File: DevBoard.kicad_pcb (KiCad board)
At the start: 4 copper layers, 100 x 83.4 mm, 130 parts, among them J1 MCUToAudio1, J10 Jumper, J11 RJ45, J12 Jumper, J13 Jumper, J14 Jumper, J15 Jumper, J16 Jumper, J17 Jumper, J18 DAC_I2S, J19 DAC_OUT, J2 MCUToAudio1, J20 DAC_Amplified, J21 DAC_Amplified, J22 Voltmeter, J23 Ground, J25 Interconnects, J26 DAC_I2S, J3 MCUToAudio2, J30 CV_Scaled_Out1, J31 AudioToMCU1, J32 AudioToMCU2, J33 CV_In2, J35 Power, J39 Ground, J4 MCUToAudio2, J40 Ground, J41 Ground, J44 Pot1, J45 Pot2, J46 Pot3, J47 Pot4, J48 CV_In1, J49 CV_Scaled_Out2, J5 MCUToCV1, J50 AudioToMCU1, J51 AudioToMCU2, J52 Pot_Out, J6 MCUToCV1, J7 MCUToCV2, J8 MCUToCV2, J9 Jumper, SW2 SW_DPDT_x2, U1 MCP6004, U2 TL074, U3 LM1117-3.3, U4 LM1117-5.0, U5 LM4040DBZ-5, U6 PCM5100APW, U8 TL072

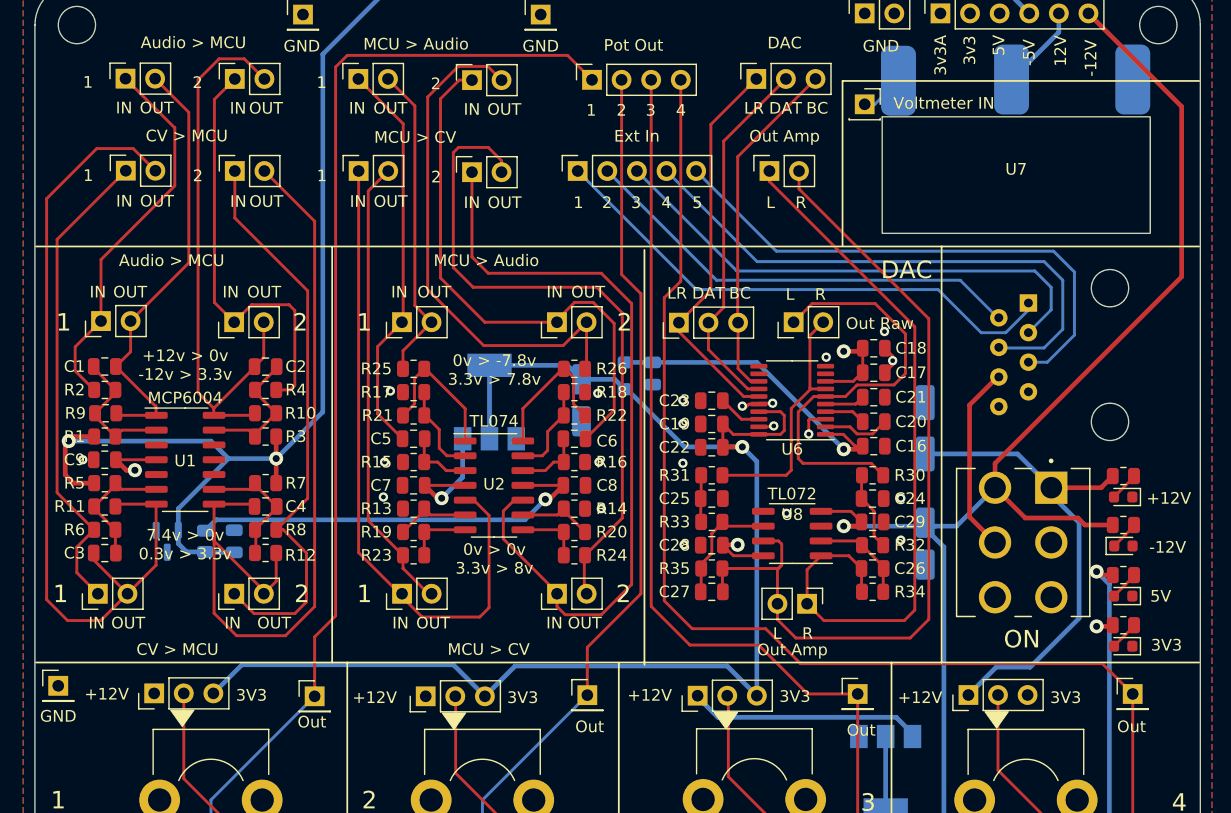
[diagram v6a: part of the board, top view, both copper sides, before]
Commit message: Layout tweaks
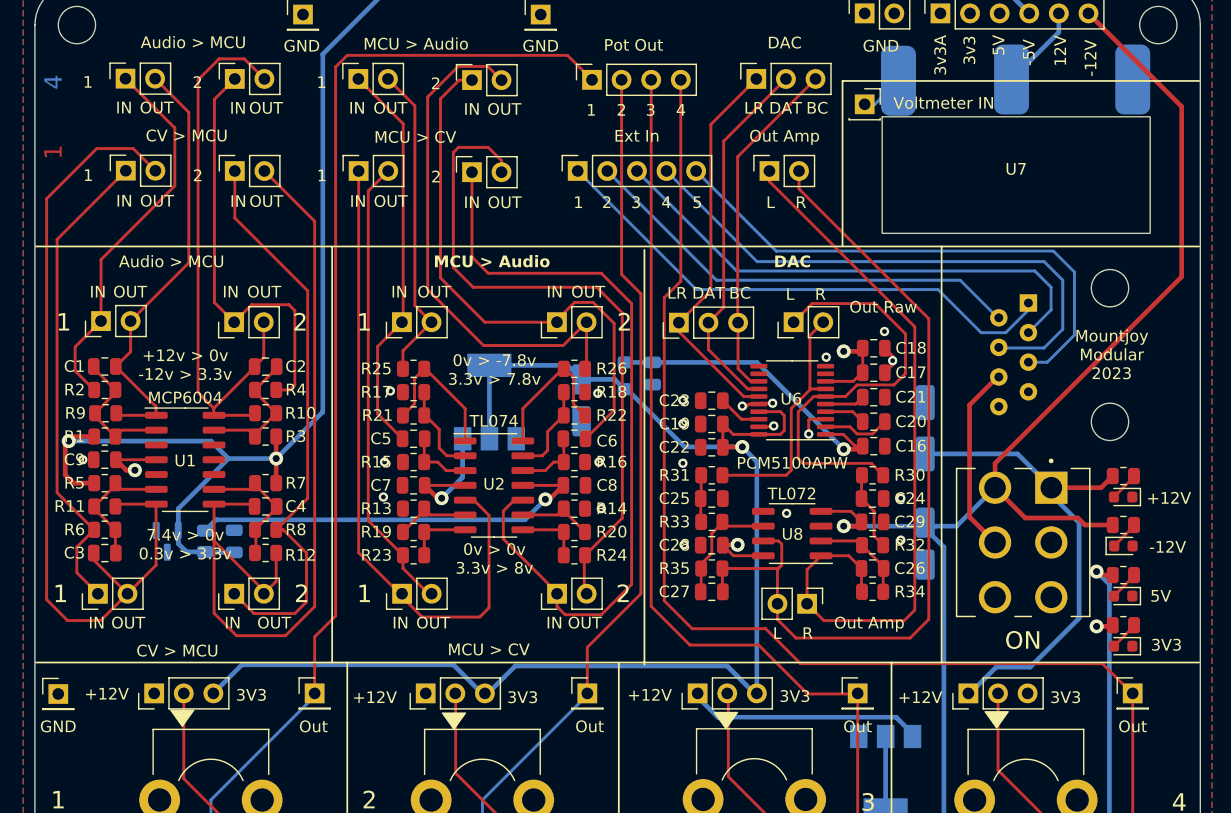
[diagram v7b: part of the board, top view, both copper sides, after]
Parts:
- added FID1: Fiducial, Custom_Footprints:4_Layer_Markers, F.Cu at (51.6, 78.1)
- moved J41 0.70 mm to (52.0, 127.6)
- moved J12 0.25 mm to (83.5, 127.5)
- moved J44 0.25 mm to (74.0, 127.5)
- moved J14 0.20 mm to (106.9, 127.5)
- moved J45 0.15 mm to (97.4, 127.5)
- moved J16 0.14 mm to (130.1, 127.5)
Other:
- board text added: "Mountjoy Modular 2023"
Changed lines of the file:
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@@
   )
   (footprint "Connector_PinHeader_2.54mm:PinHeader_1x01_P2.54mm_Vertical" (layer "F.Cu")
-    (at 52 126.9)
+    (at 52 127.6)
     (descr "Through hole straight pin header, 1x01, 2.54mm pitch, single row")
     (tags "Through hole pin header THT 1x01 2.54mm single row")
@@
   )
   (footprint "Connector_PinHeader_2.54mm:PinHeader_1x01_P2.54mm_Vertical" (layer "F.Cu")
-    (at 144.2 127.6)
+    (at 144.2 127.55)
     (descr "Through hole straight pin header, 1x01, 2.54mm pitch, single row")
     (tags "Through hole pin header THT 1x01 2.54mm single row")
@@
     (property "ki_keywords" "audio dac 2ch 32bit 384kHz")
     (attr smd)
-    (fp_text reference "U6" (at 0 -4.2 180) (layer "F.SilkS")
+    (fp_text reference "U6" (at 0.08 0.1 180) (layer "F.SilkS")
         (effects (font (size 1 1) (thickness 0.15)))
     )
-    (fp_text value "PCM5100APW" (at 0 4.2 180) (layer "F.Fab")
+    (fp_text value "PCM5100APW" (at 0 -5.4 180) (layer "F.SilkS")
         (effects (font (size 1 1) (thickness 0.15)))
     )
@@
   )
   (footprint "Connector_PinHeader_2.54mm:PinHeader_1x03_P2.54mm_Vertical" (layer "F.Cu")
-    (at 83.53 127.8 90)
+    (at 83.53 127.55 90)
     (descr "Through hole straight pin header, 1x03, 2.54mm pitch, single row")
     (tags "Through hole pin header THT 1x03 2.54mm single row")
@@
   )
   (footprint "Connector_PinHeader_2.54mm:PinHeader_1x03_P2.54mm_Vertical" (layer "F.Cu")
-    (at 106.865 127.749665 90)
+    (at 106.865 127.55 90)
     (descr "Through hole straight pin header, 1x03, 2.54mm pitch, single row")
     (tags "Through hole pin header THT 1x03 2.54mm single row")
@@
     (property "ki_keywords" "dual opamp")
     (attr smd)
-    (fp_text reference "U8" (at 0 1.635) (layer "F.SilkS")
+    (fp_text reference "U8" (at -0.02 -0.065) (layer "F.SilkS")
         (effects (font (size 1 1) (thickness 0.15)))
     )
@@
   )
   (footprint "Connector_PinHeader_2.54mm:PinHeader_1x01_P2.54mm_Vertical" (layer "F.Cu")
-    (at 97.4 127.7)
+    (at 97.4 127.55)
     (descr "Through hole straight pin header, 1x01, 2.54mm pitch, single row")
     (tags "Through hole pin header THT 1x01 2.54mm single row")
@@
   )
   (footprint "Connector_PinHeader_2.54mm:PinHeader_1x01_P2.54mm_Vertical" (layer "F.Cu")
-    (at 120.6 127.6)
+    (at 120.6 127.55)
     (descr "Through hole straight pin header, 1x01, 2.54mm pitch, single row")
     (tags "Through hole pin header THT 1x01 2.54mm single row")
@@
   )
   (footprint "Connector_PinHeader_2.54mm:PinHeader_1x01_P2.54mm_Vertical" (layer "F.Cu")
-    (at 74 127.8)
+    (at 74 127.55)
     (descr "Through hole straight pin header, 1x01, 2.54mm pitch, single row")
     (tags "Through hole pin header THT 1x01 2.54mm single row")
@@
   )
   (footprint "Connector_PinHeader_2.54mm:PinHeader_1x03_P2.54mm_Vertical" (layer "F.Cu")
-    (at 130.1 127.688915 90)
+    (at 130.1 127.55 90)
     (descr "Through hole straight pin header, 1x03, 2.54mm pitch, single row")
     (tags "Through hole pin header THT 1x03 2.54mm single row")
@@
     )
   )
+  (footprint "Custom_Footprints:4_Layer_Markers" (layer "F.Cu")
+    (at 51.6 78.1 90)
+    (property "Sheetfile" "DevBoard.kicad_sch")
+    (property "Sheetname" "")
+    (property "ki_description" "Fiducial Marker")
+    (property "ki_keywords" "fiducial marker")
+    (attr through_hole)
+    (fp_text reference "FID1" (at 0 4 90) (layer "F.SilkS") hide
+        (effects (font (size 1 1) (thickness 0.15)))
+    )
+    (fp_text value "Fiducial" (at 0 -4 90) (layer "F.Fab")
+        (effects (font (size 1 1) (thickness 0.15)))
+    )
+    (fp_text user "1" (at -3 0 90) (layer "F.Cu")
+        (effects (font (size 1.5 1.5) (thickness 0.3)))
+    )
+    (fp_text user "2" (at -1 0 90) (layer "In1.Cu")
+        (effects (font (size 1.5 1.5) (thickness 0.3)))
+    )
+    (fp_text user "3" (at 1 0 90) (layer "In2.Cu")
+        (effects (font (size 1.5 1.5) (thickness 0.3)))
+    )
+    (fp_text user "4" (at 3 0 90) (layer "B.Cu")
+        (effects (font (size 1.5 1.5) (thickness 0.3)))
+    )
+    (fp_poly
+      (pts
+        (xy 4 1)
+        (xy -4 1)
+        (xy -4 -1)
+        (xy 4 -1)
+      )
+      (stroke (width 0.1) (type solid)) (fill solid) (layer "B.Mask"))
+    (fp_poly
+      (pts
+        (xy 4 1)
+        (xy -4 1)
+        (xy -4 -1)
+        (xy 4 -1)
+      )
+      (stroke (width 0.1) (type solid)) (fill solid) (layer "F.Mask"))
+    (zone (net 0) (net_name "") (layers "*.Cu") (hatch edge 0.508)
+      (connect_pads (clearance 0))
+      (min_thickness 0.254) (filled_areas_thickness no)
+      (keepout (tracks not_allowed) (vias not_allowed) (pads allowed) (copperpour not_allowed) (footprints allowed))
+      (fill (thermal_gap 0.508) (thermal_bridge_width 0.508))
+      (polygon
+        (pts
+          (xy 52.7 74)
+          (xy 52.7 82.2)
+          (xy 50.5 82.2)
+          (xy 50.5 74)
+        )
+      )
+    )
+  )
   (footprint "Capacitor_SMD:CP_Elec_5x5.4" (layer "B.Cu")
     (at 126.4 104.8 90)
@@
     (effects (font (size 1 1) (thickness 0.15)) (justify bottom))
   )
-  (gr_text "Out" (at 144.1 131) (layer "F.SilkS")
+  (gr_text "Out" (at 144.2 131) (layer "F.SilkS")
     (effects (font (size 1 1) (thickness 0.15)) (justify bottom))
   )
@@
     (effects (font (size 1 1) (thickness 0.15)) (justify bottom))
   )
-  (gr_text "Out Amp" (at 115 124.4) (layer "F.SilkS")
+  (gr_text "Out Amp" (at 121.6 122.1) (layer "F.SilkS")
     (effects (font (size 1 1) (thickness 0.15)) (justify bottom))
   )
@@
     (effects (font (size 1 1) (thickness 0.15)) (justify bottom))
   )
-  (gr_text "ON" (at 134.7 123.7875) (layer "F.SilkS" knockout)
+  (gr_text "ON" (at 134.8 123.9) (layer "F.SilkS" knockout)
     (effects (font (size 1.5 1.5) (thickness 0.2)) (justify bottom))
   )
@@
     (effects (font (size 1 1) (thickness 0.15)) (justify bottom))
   )
-  (gr_text "Out" (at 73.765 130.600335) (layer "F.SilkS")
+  (gr_text "Out" (at 73.9 131) (layer "F.SilkS")
     (effects (font (size 1 1) (thickness 0.15)) (justify bottom))
   )
@@
     (effects (font (size 1 1) (thickness 0.15)) (justify bottom))
   )
-  (gr_text "MCU > CV" (at 85.4 124.3675) (layer "F.SilkS" knockout)
-    (effects (font (size 1 1) (thickness 0.15)) (justify left bottom))
+  (gr_text "MCU > CV" (at 85.4 124.4) (layer "F.SilkS" knockout)
+    (effects (font (size 1 1) (thickness 0.2)) (justify left bottom))
   )
   (gr_text "2" (at 63.975 83.725) (layer "F.SilkS" knockout)
@@
     (effects (font (size 1 1) (thickness 0.15)) (justify bottom))
   )
-  (gr_text "DAC" (at 124.8 92.1) (layer "F.SilkS" knockout)
-    (effects (font (size 1.5 1.5) (thickness 0.3)) (justify bottom))
+  (gr_text "DAC" (at 115 91.1) (layer "F.SilkS" knockout)
+    (effects (font (size 1 1) (thickness 0.2) bold) (justify bottom))
   )
   (gr_text "IN" (at 67.45 85.925) (layer "F.SilkS")
@@
     (effects (font (size 1 1) (thickness 0.15)) (justify bottom))
   )
-  (gr_text "CV > MCU" (at 58.7 124.3675) (layer "F.SilkS" knockout)
-    (effects (font (size 1 1) (thickness 0.15)) (justify left bottom))
+  (gr_text "CV > MCU" (at 58.7 124.5) (layer "F.SilkS" knockout)
+    (effects (font (size 1 1) (thickness 0.2)) (justify left bottom))
   )
   (gr_text "IN" (at 81.3675 122.1) (layer "F.SilkS")
@@
     (effects (font (size 1 1) (thickness 0.15)) (justify bottom))
   )
-  (gr_text "Out Raw" (at 122.5 96.4) (layer "F.SilkS")
+  (gr_text "Out Raw" (at 122.8 95) (layer "F.SilkS")
     (effects (font (size 1 1) (thickness 0.15)) (justify bottom))
   )
@@
     (effects (font (size 1 1) (thickness 0.15)) (justify bottom))
   )
-  (gr_text "GND" (at 52 130.1) (layer "F.SilkS")
+  (gr_text "Mountjoy\nModular\n2023" (at 142.4 100.7) (layer "F.SilkS" knockout)
+    (effects (font (size 1 1) (thickness 0.15)) (justify bottom))
+  )
+  (gr_text "GND" (at 52 131) (layer "F.SilkS")
     (effects (font (size 1 1) (thickness 0.15)) (justify bottom))
   )
@@
     (effects (font (size 1 1) (thickness 0.15)) (justify bottom))
   )
-  (gr_text "Audio > MCU" (at 57.2 91) (layer "F.SilkS" knockout)
-    (effects (font (size 1 1) (thickness 0.15)) (justify left bottom))
+  (gr_text "Audio > MCU" (at 57.2 91.1) (layer "F.SilkS" knockout)
+    (effects (font (size 1 1) (thickness 0.2)) (justify left bottom))
   )
   (gr_text "2" (at 84.425 83.825) (layer "F.SilkS" knockout)
@@
     (effects (font (size 1 1) (thickness 0.15)) (justify bottom))
   )
-  (gr_text "MCU > Audio" (at 84.2 91) (layer "F.SilkS" knockout)
-    (effects (font (size 1 1) (thickness 0.15)) (justify left bottom))
+  (gr_text "MCU > Audio" (at 84.2 91.1) (layer "F.SilkS" knockout)
+    (effects (font (size 1 1) (thickness 0.2) bold) (justify left bottom))
   )
   (gr_text "-5V" (at 135.9 72.561905 90) (layer "F.SilkS")
@@
     (effects (font (size 1 1) (thickness 0.15)) (justify bottom))
   )
-  (gr_text "Out" (at 120.9 131.3) (layer "F.SilkS")
+  (gr_text "Out" (at 120.6 131) (layer "F.SilkS")
     (effects (font (size 1 1) (thickness 0.15)) (justify bottom))
   )

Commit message: Preparing for production
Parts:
- FID1: value Fiducial -> 4_Layer_Marker
- moved J21 2.55 mm to (113.7, 119.9), turned to 90 degrees
- moved C17 0.14 mm to (122.0, 99.9)
- moved C24 0.13 mm to (122.0, 110.8)
- moved C26 0.13 mm to (122.0, 116.8)
- moved C29 0.13 mm to (122.0, 112.8)
- moved R30 0.13 mm to (122.0, 108.8)
- moved R32 0.13 mm to (122.0, 114.8)
- moved R34 0.13 mm to (122.0, 118.8)
- moved J8 0.12 mm to (87.5, 82.7)
- moved J26 0.12 mm to (112.0, 74.9)
- moved J31 0.10 mm to (57.8, 74.9)
- moved J51 0.09 mm to (67.2, 74.9)
- moved J1 0.08 mm to (77.8, 74.9)
- moved R9 0.07 mm to (56.0, 103.5)
- moved C16 0.07 mm to (122.0, 106.4)
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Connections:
- net /Interconnect4_GATE renamed /Interconnect4
- net /Interconnect5_CV renamed /Interconnect5
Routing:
- net /Pot1: track 97.6 -> 105.3 mm
- net /Pot2: track 75.1 -> 82.8 mm
- net /MCUToEurorack/CV2_In: track 66.7 -> 69.3 mm
- net /DAC/DAC_OUT_AMP_R: track 72.9 -> 75.6 mm
- net /DAC/DAC_OUT_AMP_L: track 63.6 -> 61.2 mm
- net +12V: track 246.4 -> 244.2 mm
- net Net-(R22-Pad1): track 12.6 -> 13.9 mm
- net Net-(R21-Pad1): track 12.5 -> 13.8 mm
- net GND: track 8.91 -> 9.93 mm
- net +3.3VA: track 147.2 -> 147.9 mm
- net /Pot4: track 113.6 -> 114.3 mm
- net -12V: track 254.8 -> 255.4 mm
- net /EurorackToMCU/CV_Scaled_Out1: track 72.4 -> 71.8 mm
- net /EurorackToMCU/CV_In1: track 41.4 -> 42.0 mm
- net Net-(U1A--): track 11.9 -> 11.4 mm
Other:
- board text added: "JLCJLCJLCJLC"
